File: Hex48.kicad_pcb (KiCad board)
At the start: 2 copper layers, 77.9 x 90 mm, 24 parts, among them J1 Conn_02x24_Counter_Clockwise, J10 Conn_02x08_Odd_Even, J11 Conn_02x08_Odd_Even, J12 Conn_02x08_Odd_Even, J13 Conn_02x08_Odd_Even, J14 Conn_02x08_Odd_Even, J2 Conn_02x24_Odd_Even, J3 Conn_02x24_Odd_Even, J4 Conn_02x02_Odd_Even, J5 Conn_02x02_Odd_Even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

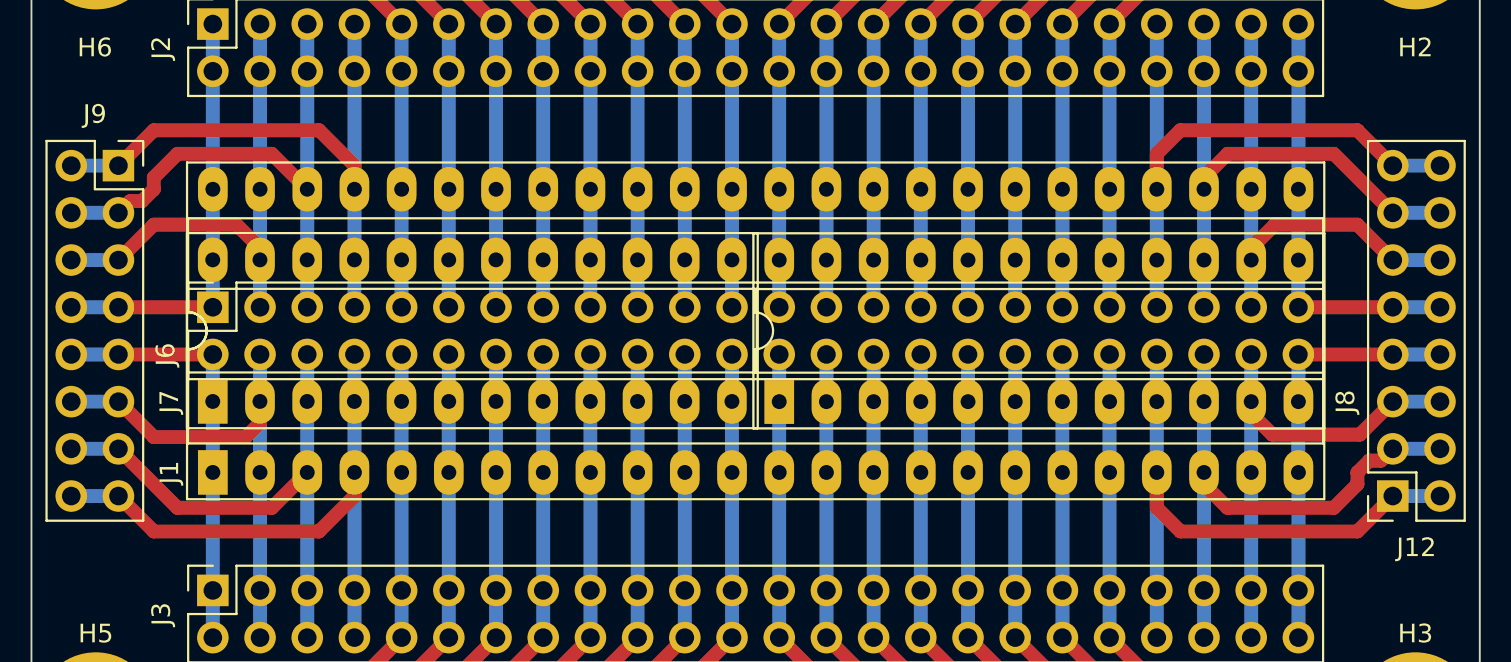
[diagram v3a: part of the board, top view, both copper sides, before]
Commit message: Move eight tracks just a little bit further from the sockets.
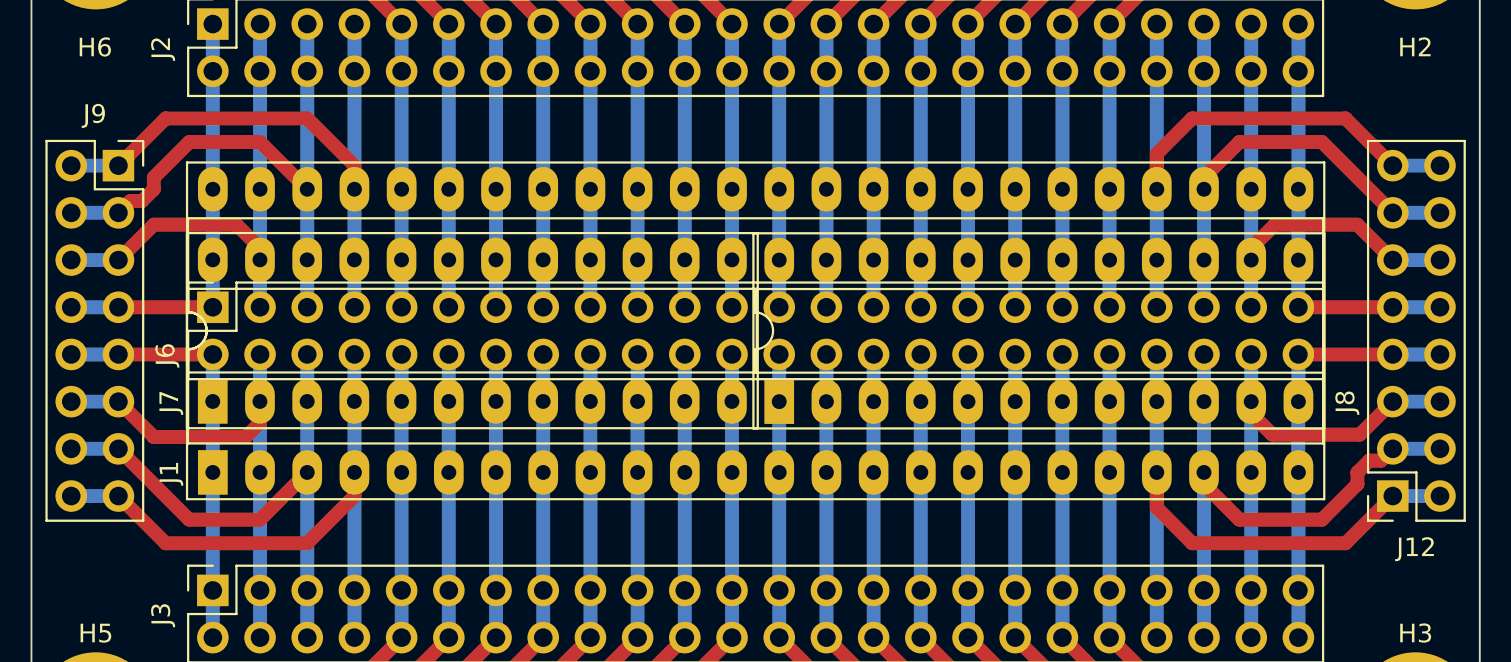
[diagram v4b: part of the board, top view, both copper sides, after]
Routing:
- net /pin27: track 30.4 -> 30.9 mm
- net /pin46: track 30.4 -> 30.9 mm
- net /pin28: track 33.7 -> 34.2 mm
- net /pin45: track 33.3 -> 33.9 mm
- net /pin22: track 30.8 -> 31.3 mm
- net /pin4: track 33.3 -> 33.9 mm
- net /pin21: track 33.7 -> 34.2 mm
- net /pin3: track 30.0 -> 30.6 mm
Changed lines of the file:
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@@
 	)
 	(segment
-		(start 156.845 81.915)
-		(end 153.67 78.74)
+		(start 161.29 82.55)
+		(end 157.48 82.55)
 		(width 0.75)
 		(layer "F.Cu")
@@
 	)
 	(segment
-		(start 161.925 81.915)
-		(end 156.845 81.915)
+		(start 163.83 80.01)
+		(end 161.29 82.55)
 		(width 0.75)
 		(layer "F.Cu")
@@
 	)
 	(segment
-		(start 163.83 80.01)
-		(end 161.925 81.915)
+		(start 157.48 82.55)
+		(end 153.67 78.74)
 		(width 0.75)
 		(layer "F.Cu")
@@
 	)
 	(segment
-		(start 210.82 83.185)
-		(end 209.55 81.915)
+		(start 219.71 83.82)
+		(end 211.455 83.82)
 		(width 0.75)
 		(layer "F.Cu")
@@
 	)
 	(segment
-		(start 209.55 81.915)
-		(end 209.55 80.01)
+		(start 211.455 83.82)
+		(end 209.55 81.915)
 		(width 0.75)
 		(layer "F.Cu")
@@
 	)
 	(segment
-		(start 220.345 83.185)
-		(end 210.82 83.185)
+		(start 209.55 81.915)
+		(end 209.55 80.01)
 		(width 0.75)
 		(layer "F.Cu")
@@
 	(segment
 		(start 222.25 81.28)
-		(end 220.345 83.185)
+		(end 219.71 83.82)
 		(width 0.75)
 		(layer "F.Cu")
@@
 	)
 	(segment
-		(start 213.36 81.915)
-		(end 212.09 80.645)
+		(start 222.25 78.74)
+		(end 221.615 79.375)
 		(width 0.75)
 		(layer "F.Cu")
@@
 	)
 	(segment
-		(start 219.075 81.915)
-		(end 213.36 81.915)
+		(start 213.995 82.55)
+		(end 212.09 80.645)
 		(width 0.75)
 		(layer "F.Cu")
@@
 	)
 	(segment
-		(start 212.09 80.645)
-		(end 212.09 80.01)
+		(start 220.345 80.645)
+		(end 218.44 82.55)
 		(width 0.75)
 		(layer "F.Cu")
@@
 	)
 	(segment
-		(start 220.98 79.375)
-		(end 220.345 80.01)
+		(start 221.615 79.375)
+		(end 220.98 79.375)
 		(width 0.75)
 		(layer "F.Cu")
@@
 	)
 	(segment
-		(start 220.345 80.01)
-		(end 220.345 80.645)
+		(start 218.44 82.55)
+		(end 213.995 82.55)
 		(width 0.75)
 		(layer "F.Cu")
@@
 	)
 	(segment
-		(start 220.345 80.645)
-		(end 219.075 81.915)
+		(start 220.98 79.375)
+		(end 220.345 80.01)
 		(width 0.75)
 		(layer "F.Cu")
@@
 	)
 	(segment
-		(start 221.615 79.375)
-		(end 220.98 79.375)
+		(start 212.09 80.645)
+		(end 212.09 80.01)
 		(width 0.75)
 		(layer "F.Cu")
@@
 	)
 	(segment
-		(start 222.25 78.74)
-		(end 221.615 79.375)
+		(start 220.345 80.01)
+		(end 220.345 80.645)
 		(width 0.75)
 		(layer "F.Cu")
@@
 	)
 	(segment
-		(start 222.25 63.5)
-		(end 220.345 61.595)
+		(start 219.71 60.96)
+		(end 211.455 60.96)
 		(width 0.75)
 		(layer "F.Cu")
@@
 	)
 	(segment
-		(start 220.345 61.595)
-		(end 210.82 61.595)
+		(start 209.55 62.865)
+		(end 209.55 64.77)
 		(width 0.75)
 		(layer "F.Cu")
@@
 	)
 	(segment
-		(start 209.55 62.865)
-		(end 209.55 64.77)
+		(start 222.25 63.5)
+		(end 219.71 60.96)
 		(width 0.75)
 		(layer "F.Cu")
@@
 	)
 	(segment
-		(start 210.82 61.595)
+		(start 211.455 60.96)
 		(end 209.55 62.865)
 		(width 0.75)
@@
 	)
 	(segment
-		(start 212.09 64.135)
-		(end 212.09 64.77)
+		(start 218.44 62.23)
+		(end 213.995 62.23)
 		(width 0.75)
 		(layer "F.Cu")
@@
 	)
 	(segment
-		(start 222.25 66.04)
-		(end 219.075 62.865)
+		(start 213.995 62.23)
+		(end 212.09 64.135)
 		(width 0.75)
 		(layer "F.Cu")
@@
 	)
 	(segment
-		(start 219.075 62.865)
-		(end 213.36 62.865)
+		(start 222.25 66.04)
+		(end 218.44 62.23)
 		(width 0.75)
 		(layer "F.Cu")
@@
 	)
 	(segment
-		(start 213.36 62.865)
-		(end 212.09 64.135)
+		(start 212.09 64.135)
+		(end 212.09 64.77)
 		(width 0.75)
 		(layer "F.Cu")
@@
 	)
 	(segment
-		(start 166.37 81.28)
-		(end 166.37 80.01)
+		(start 153.67 81.28)
+		(end 156.21 83.82)
 		(width 0.75)
 		(layer "F.Cu")
@@
 	)
 	(segment
-		(start 155.575 83.185)
-		(end 164.465 83.185)
+		(start 166.37 81.28)
+		(end 166.37 80.01)
 		(width 0.75)
 		(layer "F.Cu")
@@
 	)
 	(segment
-		(start 153.67 81.28)
-		(end 155.575 83.185)
+		(start 163.83 83.82)
+		(end 166.37 81.28)
 		(width 0.75)
 		(layer "F.Cu")
@@
 	)
 	(segment
-		(start 164.465 83.185)
-		(end 166.37 81.28)
+		(start 156.21 83.82)
+		(end 163.83 83.82)
 		(width 0.75)
 		(layer "F.Cu")
@@
 	)
 	(segment
-		(start 156.845 62.865)
+		(start 157.48 62.23)
 		(end 155.575 64.135)
 		(width 0.75)
@@
 	)
 	(segment
-		(start 154.94 65.405)
-		(end 154.305 65.405)
+		(start 154.305 65.405)
+		(end 153.67 66.04)
 		(width 0.75)
 		(layer "F.Cu")
@@
 	)
 	(segment
-		(start 163.83 64.77)
-		(end 161.925 62.865)
+		(start 155.575 64.135)
+		(end 155.575 64.77)
 		(width 0.75)
 		(layer "F.Cu")
@@
 	)
 	(segment
-		(start 161.925 62.865)
-		(end 156.845 62.865)
+		(start 163.83 64.77)
+		(end 161.29 62.23)
 		(width 0.75)
 		(layer "F.Cu")
@@
 	)
 	(segment
-		(start 155.575 64.135)
-		(end 155.575 64.77)
+		(start 161.29 62.23)
+		(end 157.48 62.23)
 		(width 0.75)
 		(layer "F.Cu")
@@
 	)
 	(segment
-		(start 154.305 65.405)
-		(end 153.67 66.04)
+		(start 154.94 65.405)
+		(end 154.305 65.405)
 		(width 0.75)
 		(layer "F.Cu")
@@
 	)
 	(segment
-		(start 155.575 61.595)
-		(end 164.465 61.595)
+		(start 163.83 60.96)
+		(end 166.37 63.5)
 		(width 0.75)
 		(layer "F.Cu")
@@
 	)
 	(segment
-		(start 153.67 63.5)
-		(end 155.575 61.595)
+		(start 156.21 60.96)
+		(end 163.83 60.96)
 		(width 0.75)
 		(layer "F.Cu")
@@
 	)
 	(segment
-		(start 164.465 61.595)
-		(end 166.37 63.5)
+		(start 166.37 63.5)
+		(end 166.37 64.77)
 		(width 0.75)
 		(layer "F.Cu")
@@
 	)
 	(segment
-		(start 166.37 63.5)
-		(end 166.37 64.77)
+		(start 153.67 63.5)
+		(end 156.21 60.96)
 		(width 0.75)
 		(layer "F.Cu")

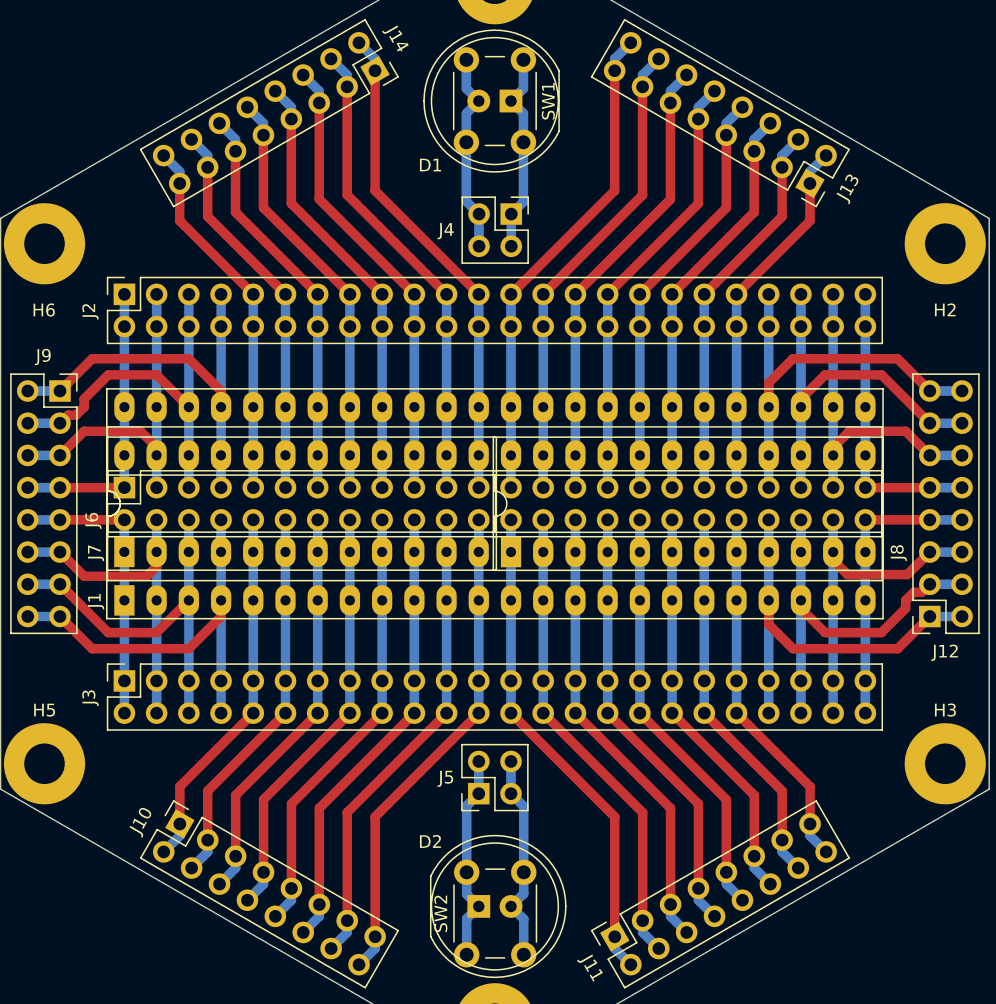
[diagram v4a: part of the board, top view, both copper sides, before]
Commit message: Add pin numbers to silkscreen.
Just a few, because the true pin number will change if you fit a 40-pin chip, or two 24-pin chips, or three 16-pin chips. Better to follow the tracks visually.
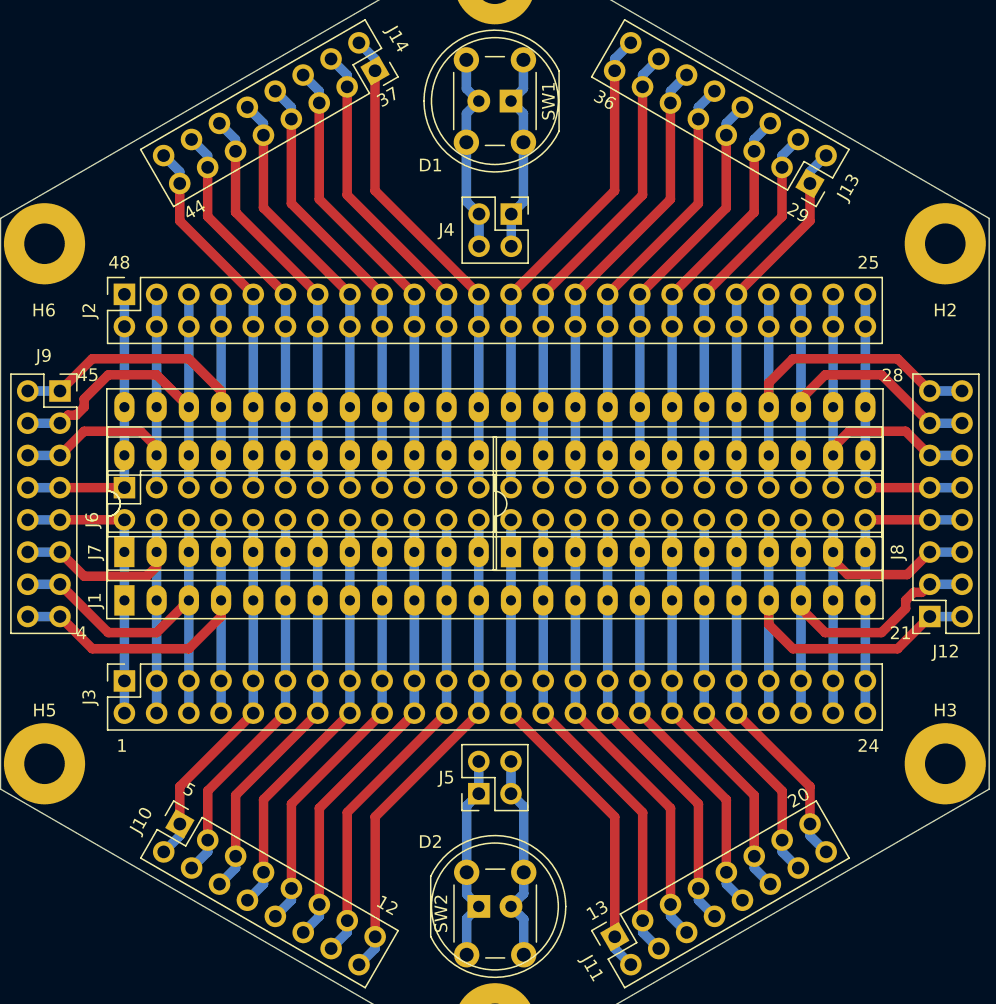
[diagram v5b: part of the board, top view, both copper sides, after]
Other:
- board text added: "1"
- board text added: "12"
- board text added: "13"
- board text added: "20"
- board text added: "21"
- board text added: "24"
- board text added: "25"
- board text added: "28"
- board text added: "29"
- board text added: "36"
- board text added: "37"
- board text added: "4"
- board text added: "44"
- board text added: "45"
- board text added: "48"
- board text added: "5"
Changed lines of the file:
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@@
 		(layer "Edge.Cuts")
+	)
+	(gr_text "37"
+		(at 179.07 41.275 30)
+		(layer "F.SilkS")
+		(effects
+			(font
+				(size 1 1)
+				(thickness 0.15)
+			)
+			(justify left bottom)
+		)
+	)
+	(gr_text "29"
+		(at 210.82 49.53 330)
+		(layer "F.SilkS")
+		(effects
+			(font
+				(size 1 1)
+				(thickness 0.15)
+			)
+			(justify left bottom)
+		)
+	)
+	(gr_text "21"
+		(at 219.075 83.185 0)
+		(layer "F.SilkS")
+		(effects
+			(font
+				(size 1 1)
+				(thickness 0.15)
+			)
+			(justify left bottom)
+		)
+	)
+	(gr_text "1"
+		(at 158.115 92.075 0)
+		(layer "F.SilkS")
+		(effects
+			(font
+				(size 1 1)
+				(thickness 0.15)
+			)
+			(justify left bottom)
+		)
+	)
+	(gr_text "24"
+		(at 216.535 92.075 0)
+		(layer "F.SilkS")
+		(effects
+			(font
+				(size 1 1)
+				(thickness 0.15)
+			)
+			(justify left bottom)
+		)
+	)
+	(gr_text "20"
+		(at 211.455 96.52 30)
+		(layer "F.SilkS")
+		(effects
+			(font
+				(size 1 1)
+				(thickness 0.15)
+			)
+			(justify left bottom)
+		)
+	)
+	(gr_text "4"
+		(at 154.94 83.185 0)
+		(layer "F.SilkS")
+		(effects
+			(font
+				(size 1 1)
+				(thickness 0.15)
+			)
+			(justify left bottom)
+		)
+	)
+	(gr_text "12"
+		(at 178.435 104.14 330)
+		(layer "F.SilkS")
+		(effects
+			(font
+				(size 1 1)
+				(thickness 0.15)
+			)
+			(justify left bottom)
+		)
+	)
+	(gr_text "36"
+		(at 195.58 40.64 330)
+		(layer "F.SilkS")
+		(effects
+			(font
+				(size 1 1)
+				(thickness 0.15)
+			)
+			(justify left bottom)
+		)
+	)
+	(gr_text "5"
+		(at 163.195 95.25 330)
+		(layer "F.SilkS")
+		(effects
+			(font
+				(size 1 1)
+				(thickness 0.15)
+			)
+			(justify left bottom)
+		)
+	)
+	(gr_text "45"
+		(at 155 62.835 0)
+		(layer "F.SilkS")
+		(effects
+			(font
+				(size 1 1)
+				(thickness 0.15)
+			)
+			(justify left bottom)
+		)
+	)
+	(gr_text "25"
+		(at 216.535 53.975 0)
+		(layer "F.SilkS")
+		(effects
+			(font
+				(size 1 1)
+				(thickness 0.15)
+			)
+			(justify left bottom)
+		)
+	)
+	(gr_text "28"
+		(at 218.44 62.865 0)
+		(layer "F.SilkS")
+		(effects
+			(font
+				(size 1 1)
+				(thickness 0.15)
+			)
+			(justify left bottom)
+		)
+	)
+	(gr_text "44"
+		(at 163.83 50.165 30)
+		(layer "F.SilkS")
+		(effects
+			(font
+				(size 1 1)
+				(thickness 0.15)
+			)
+			(justify left bottom)
+		)
+	)
+	(gr_text "13"
+		(at 195.58 105.41 30)
+		(layer "F.SilkS")
+		(effects
+			(font
+				(size 1 1)
+				(thickness 0.15)
+			)
+			(justify left bottom)
+		)
+	)
+	(gr_text "48"
+		(at 157.48 53.975 0)
+		(layer "F.SilkS")
+		(effects
+			(font
+				(size 1 1)
+				(thickness 0.15)
+			)
+			(justify left bottom)
+		)
 	)
 	(dimension

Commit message: Add silkscreen and back copper text.
KiCad logo, OSHW logo, WEEE logo, name, designers name, date. That Twitter handle is going to look very old very quickly.
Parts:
- added REF**: OSHW-Symbol_6.7x6mm_SilkScreen, Symbol:OSHW-Symbol_6.7x6mm_SilkScreen, F.Cu at (158.8, 48.9)
- added REF**: KiCad-Logo2_5mm_SilkScreen, Symbol:KiCad-Logo2_5mm_SilkScreen, F.Cu at (200.0, 50.8)
- added REF**: WEEE-Logo_4.2x6mm_SilkScreen, Symbol:WEEE-Logo_4.2x6mm_SilkScreen, F.Cu at (217.2, 95.9)
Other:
- board text added: "@anachrocomputer"
- board text added: "HEX48"
- board text added: "John Honniball"
- board text added: "©2024"
